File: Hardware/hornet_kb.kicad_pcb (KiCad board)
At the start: 2 copper layers, 195.1 x 100.9 mm, 133 parts, among them J1 Conn_ST_STDC14, J10 USB_C_Receptacle_USB2.0, J2 Conn_01x03, SW1 ESC, SW10 TAB, SW11 Q, SW12 W, SW13 E, SW14 R, SW15 T, SW17 M1, SW18 CAPS, SW19 A, SW2 `, SW20 S, SW21 D, SW22 F, SW23 G, SW25 M2, SW26 M3, SW28 SHIFT, SW29 CTRL, SW3 1, SW31 Z, SW32 WIN, SW34 X, SW35 FN, SW37 C, SW38 ALT, SW4 2, SW40 V, SW41 SPACE, SW43 B, SW44 DEL, SW5 3, SW6 4, SW7 5, SW8 6, SW9 M0, U1 nRF52840, U2 BQ24040, U3 BQ51050BRHL, U4 AP22814BW5, Y1 32.768kHz, Y2 32MHz

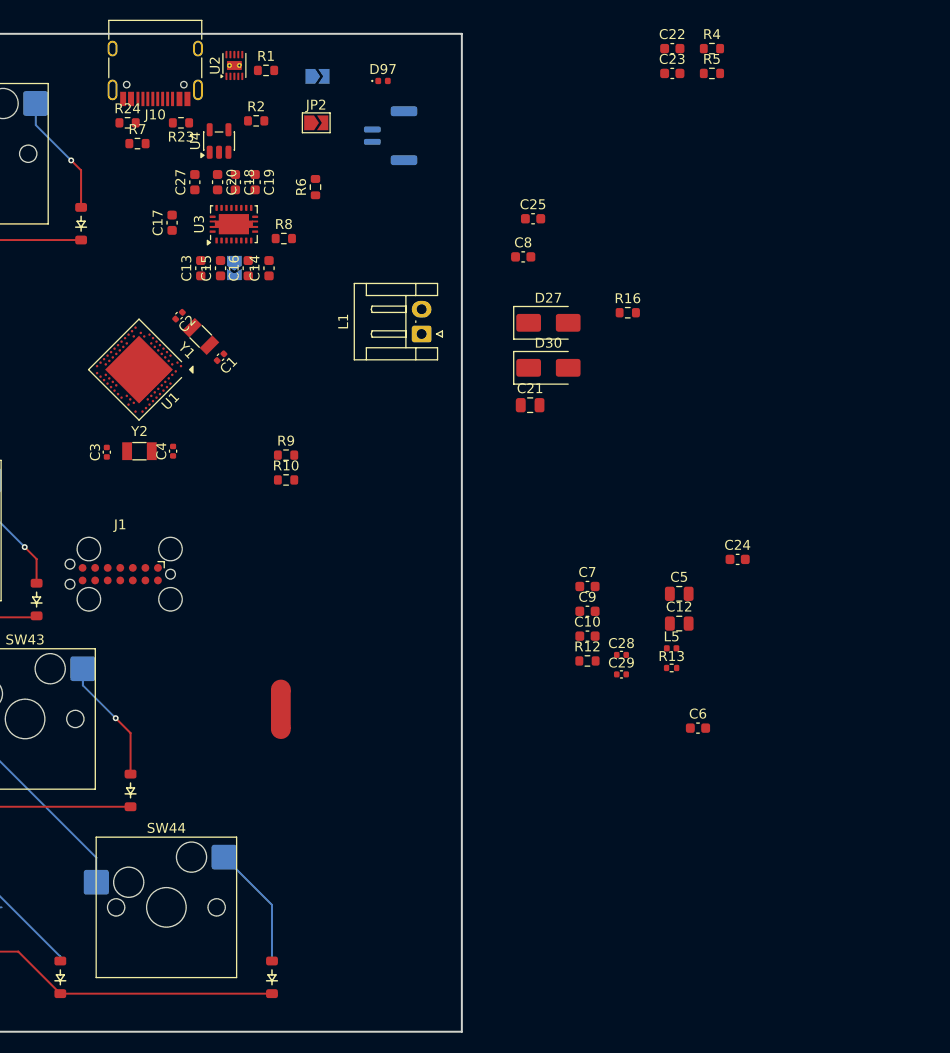
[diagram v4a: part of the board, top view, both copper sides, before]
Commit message: added extra decoupling caps to the mcu VDD pins
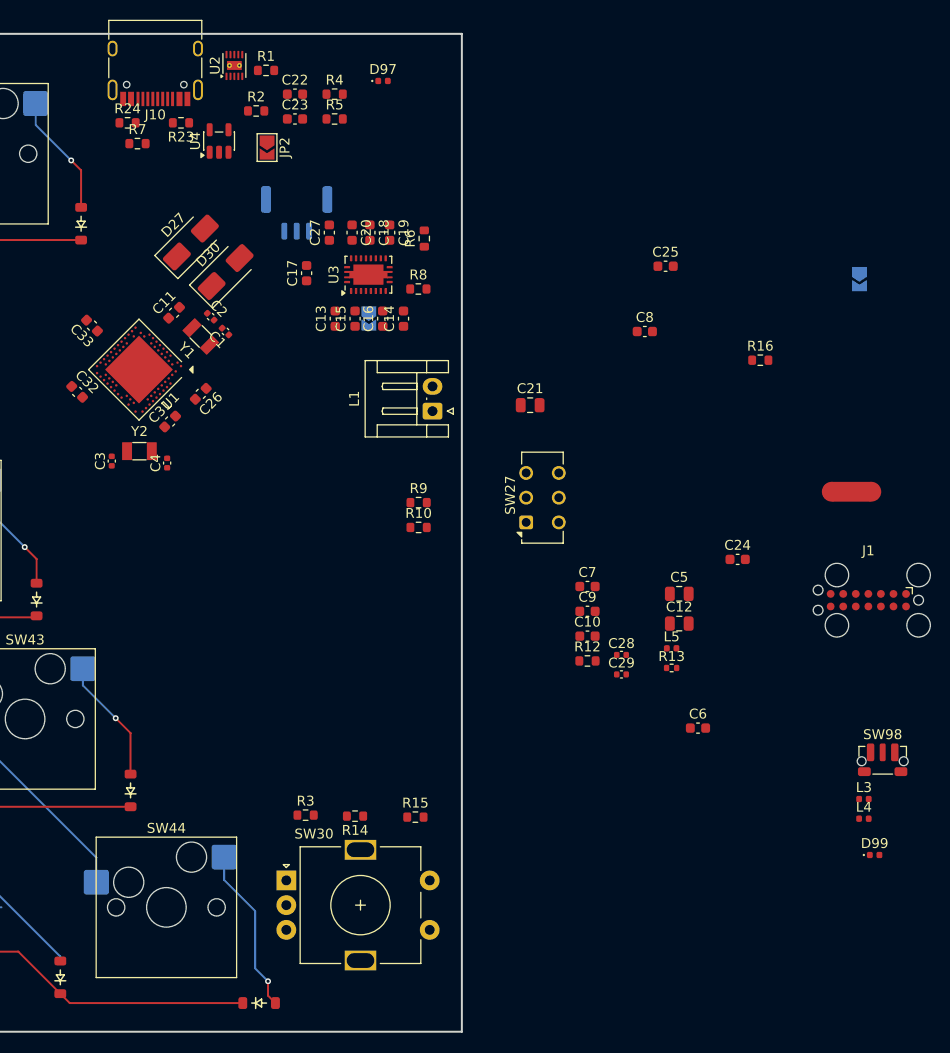
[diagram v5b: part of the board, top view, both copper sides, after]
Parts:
- added C11: 100pF, Capacitor_SMD:C_0603_1608Metric, F.Cu at (205.2, 73.2)
- added C26: 100pF, Capacitor_SMD:C_0603_1608Metric, F.Cu at (207.9, 81.4)
- added C31: 100pF, Capacitor_SMD:C_0603_1608Metric, F.Cu at (204.8, 84.2)
- added C32: 100pF, Capacitor_SMD:C_0603_1608Metric, F.Cu at (195.4, 81.2)
- added C33: 100pF, Capacitor_SMD:C_0603_1608Metric, F.Cu at (196.9, 74.5)
- added D99: QI_CHG, LED_SMD:LED_0402_1005Metric, F.Cu at (276.1, 128.1)
- added L3: 10uH, Inductor_SMD:L_0402_1005Metric, F.Cu at (275.0, 122.4)
- added L4: 25uH, Inductor_SMD:L_0402_1005Metric, F.Cu at (275.0, 124.4)
- added R14: 10k, Resistor_SMD:R_0603_1608Metric, F.Cu at (223.5, 124.1)
- added R15: 10k, Resistor_SMD:R_0603_1608Metric, F.Cu at (229.6, 124.2)
- added R3: 10k, Resistor_SMD:R_0603_1608Metric, F.Cu at (218.5, 124.0)
- added SW27: SW_DPDT_x2, Button_Switch_THT:SW_CK_JS202011CQN_DPDT_Straight, F.Cu at (240.8, 94.4)
- added SW30: Rot_Enc, Rotary_Encoder:RotaryEncoder_Alps_EC11E-Switch_Vertical_H20mm, F.Cu at (216.6, 130.6)
- added SW98: SW_Push, Button_Switch_SMD:SW_Push_1P1T-MP_NO_Horizontal_Alps_SKRTLAE010, F.Cu at (276.9, 118.6)
- C22: value 10uF -> 1uF
- J2: footprint Connector_JST:JST_GH_SM02B-GHS-TB_1x02-1MP_P1.25mm_Horizontal -> Connector_JST:JST_GH_SM03B-GHS-TB_1x03-1MP_P1.25mm_Horizontal
- moved J1 75.7 mm to (275.4, 102.3)
- moved NT1 61.8 mm to (273.7, 91.3), turned to 180 degrees
- moved JP1 58.5 mm to (274.5, 69.8), turned to -90 degrees
- moved C22 38.4 mm to (217.5, 51.1)
- moved C23 38.4 mm to (217.5, 53.6)
- moved R4 38.4 mm to (221.5, 51.1)
- moved R5 38.4 mm to (221.5, 53.6)
- moved D27 37.1 mm to (206.9, 66.1), turned to 45 degrees
- moved D30 34.0 mm to (210.5, 69.1), turned to 45 degrees
- moved C13 14.5 mm to (221.5, 73.8)
- moved C15 14.5 mm to (223.5, 73.8)
- moved C17 14.5 mm to (218.6, 69.2)
- moved U3 14.5 mm to (224.9, 69.4)
- moved C18 14.5 mm to (225.0, 65.1)
- moved C19 14.5 mm to (227.0, 65.1)
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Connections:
- C3 pad 1: GND1 -> GND
- C4 pad 1: GND1 -> GND
- U1 pad AC17: /R_COL_6 -> unconnected-(U1-P0.21-PadAC17)
- U1 pad AD10: unconnected-(U1-P0.15-PadAD10) -> /R_COL_7
- U1 pad AD12: unconnected-(U1-P0.17-PadAD12) -> /R_COL_6
- U1 pad AD16: /R_COL_7 -> /R_ROW_2
- U1 pad AD8: unconnected-(U1-P0.13-PadAD8) -> /R_ROW_0
- U1 pad V23: /R_ROW_2 -> unconnected-(U1-P1.03-PadV23)
- U1 pad Y23: /R_ROW_0 -> unconnected-(U1-P1.01-PadY23)
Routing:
- net Net-(D44-A): track 12.5 -> 16.9 mm, vias 0 -> 1
- net /R_ROW_4: track 156.1 -> 153.6 mm

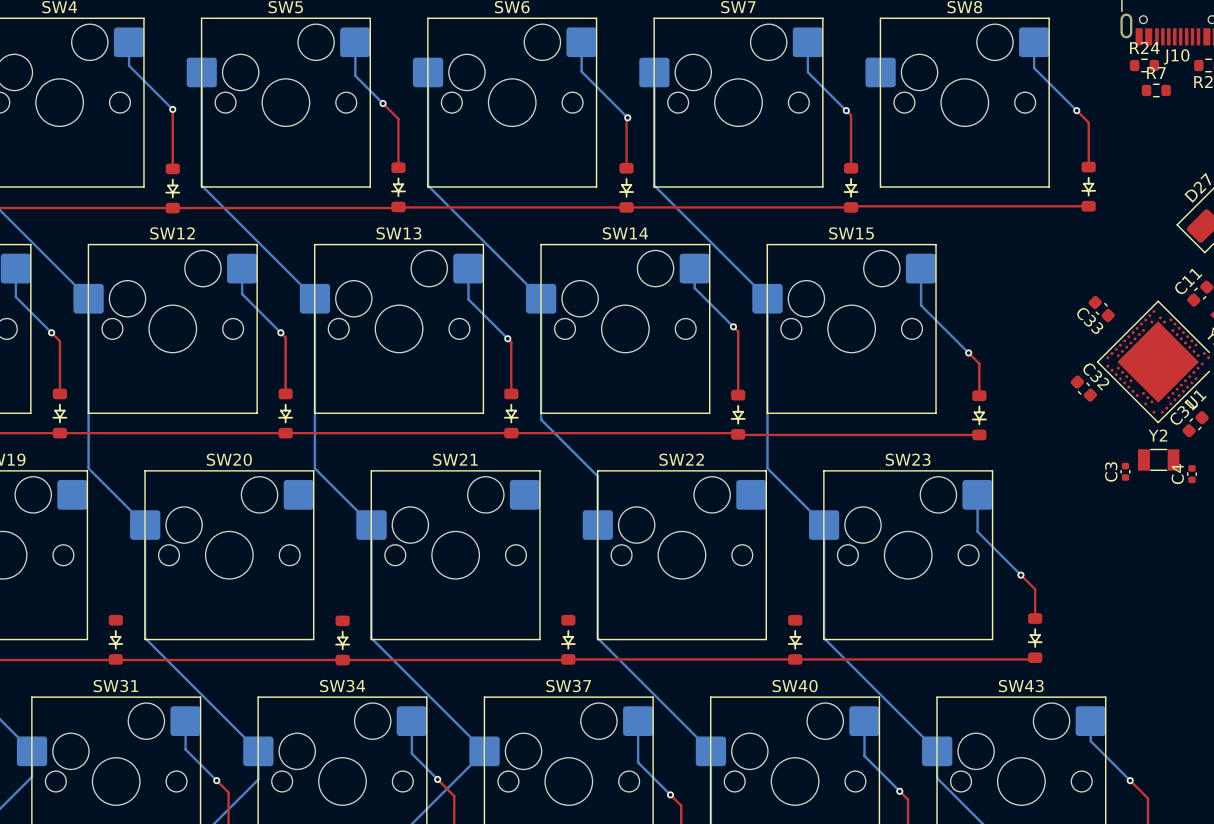
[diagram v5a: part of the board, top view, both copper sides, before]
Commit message: changed pin allocations for keys based on physical location
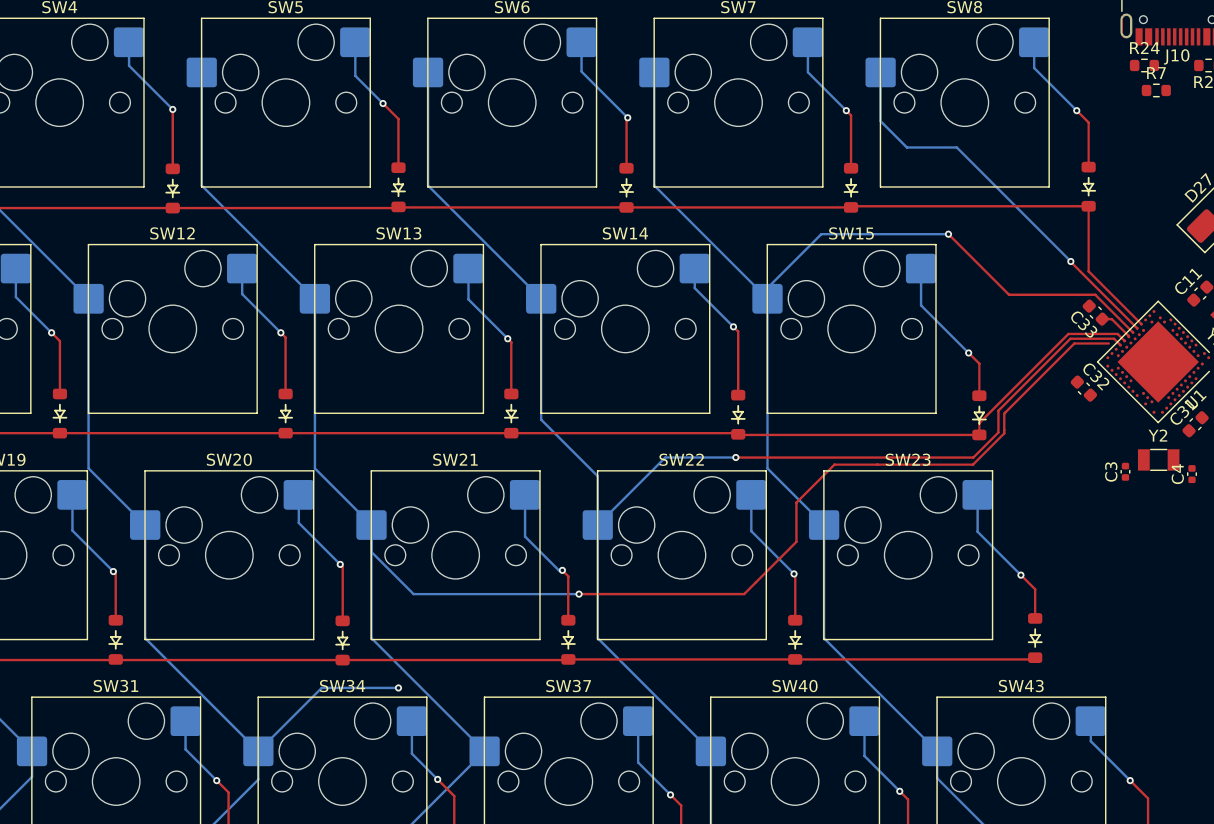
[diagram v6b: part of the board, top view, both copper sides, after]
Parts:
- moved C33 0.58 mm to (196.4, 74.8)
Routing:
- net /R_COL_4: track 91.0 -> 168.5 mm, vias 0 -> 1
- net /R_COL_5: track 87.0 -> 138.8 mm, vias 0 -> 1
- net /R_COL_6: track 92.0 -> 129.0 mm, vias 0 -> 1
- net /R_COL_7: track 0.00 -> 32.9 mm, vias 0 -> 1
- net /R_ROW_2: track 124.1 -> 140.7 mm
- net /R_COL_3: track 93.0 -> 107.0 mm, vias 0 -> 1
- net Net-(D21-A): track 0.00 -> 12.2 mm, vias 0 -> 1
- net Net-(D20-A): track 0.00 -> 12.1 mm, vias 0 -> 1
- net Net-(D22-A): track 0.00 -> 12.1 mm, vias 0 -> 1
- net Net-(D19-A): track 0.00 -> 12.1 mm, vias 0 -> 1
- net /R_ROW_0: track 134.4 -> 146.2 mm
- net VDD: track 0.00 -> 2.88 mm

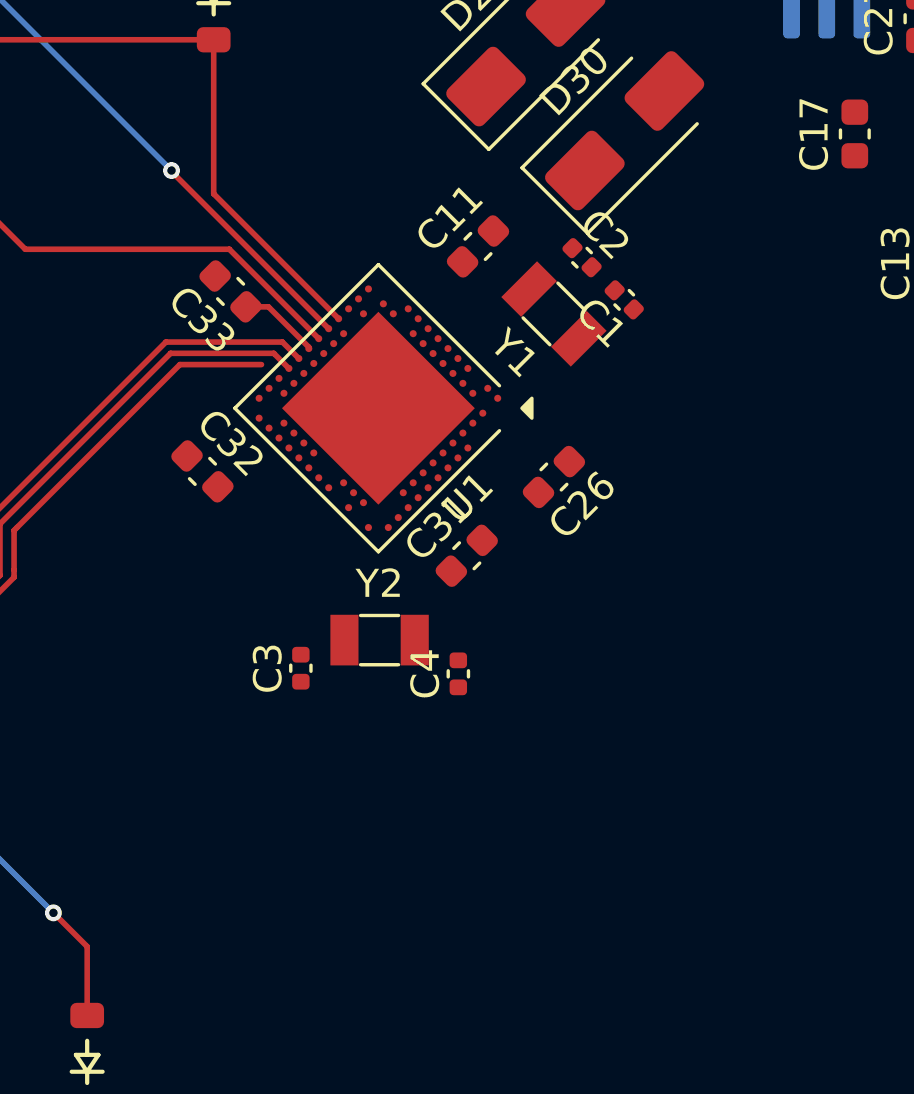
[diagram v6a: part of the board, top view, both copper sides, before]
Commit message: move MCU to prioritize BLE routing
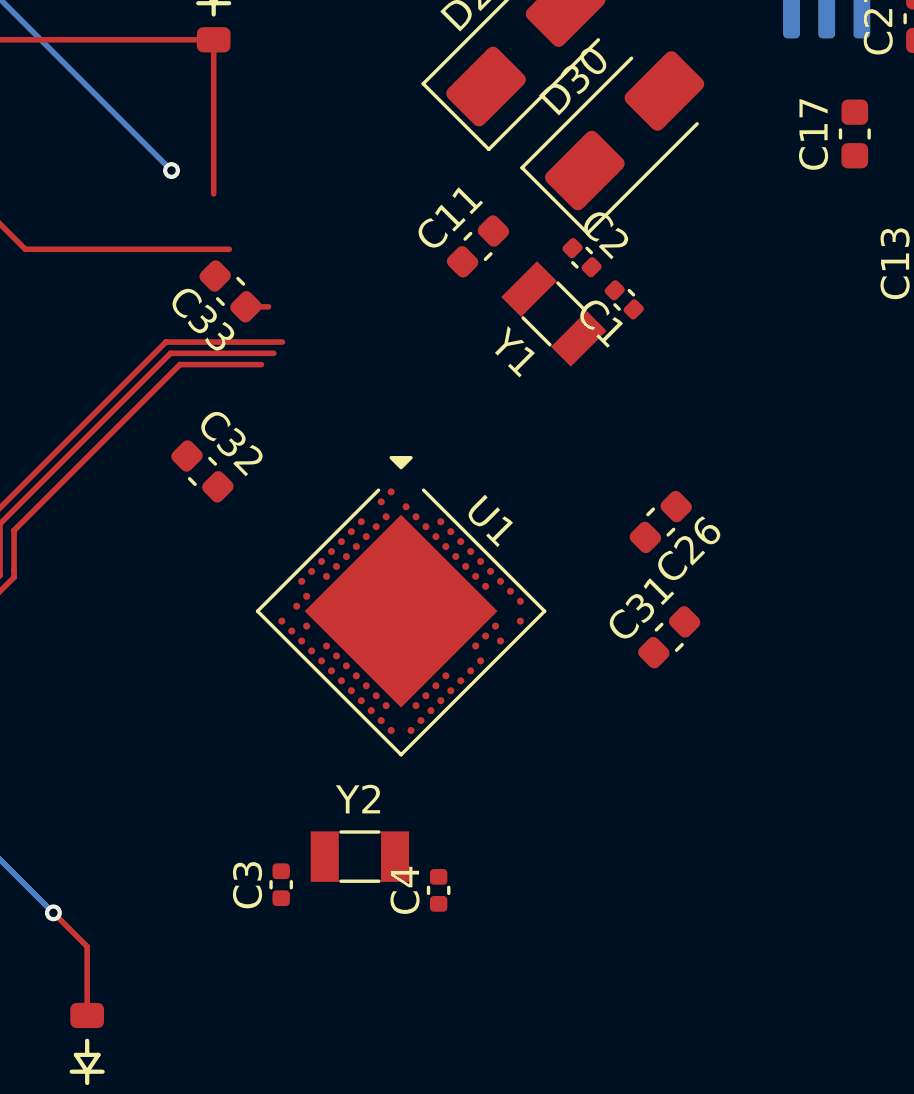
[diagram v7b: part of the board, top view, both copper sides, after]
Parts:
- moved C31 7.76 mm to (212.0, 87.1)
- moved Y2 7.73 mm to (201.0, 94.9)
- moved C3 7.73 mm to (198.2, 95.9)
- moved C4 7.73 mm to (203.8, 96.1)
- moved U1 7.26 mm to (202.5, 86.2), turned to -45 degrees
- moved C26 4.12 mm to (211.7, 83.0)
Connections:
- U1 pad AC19: /R_COL_4 -> unconnected-(U1-P0.23-PadAC19)
- U1 pad AD20: /R_COL_3 -> /R_COL_4
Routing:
- net /R_COL_7: track 32.9 -> 25.0 mm
- net /R_ROW_0: track 146.2 -> 139.9 mm
- net /R_COL_6: track 129.0 -> 124.5 mm
- net VDD: track 2.88 -> 0.80 mm
- net /R_ROW_2: track 140.7 -> 139.9 mm
- net /R_COL_5: track 138.8 -> 138.1 mm

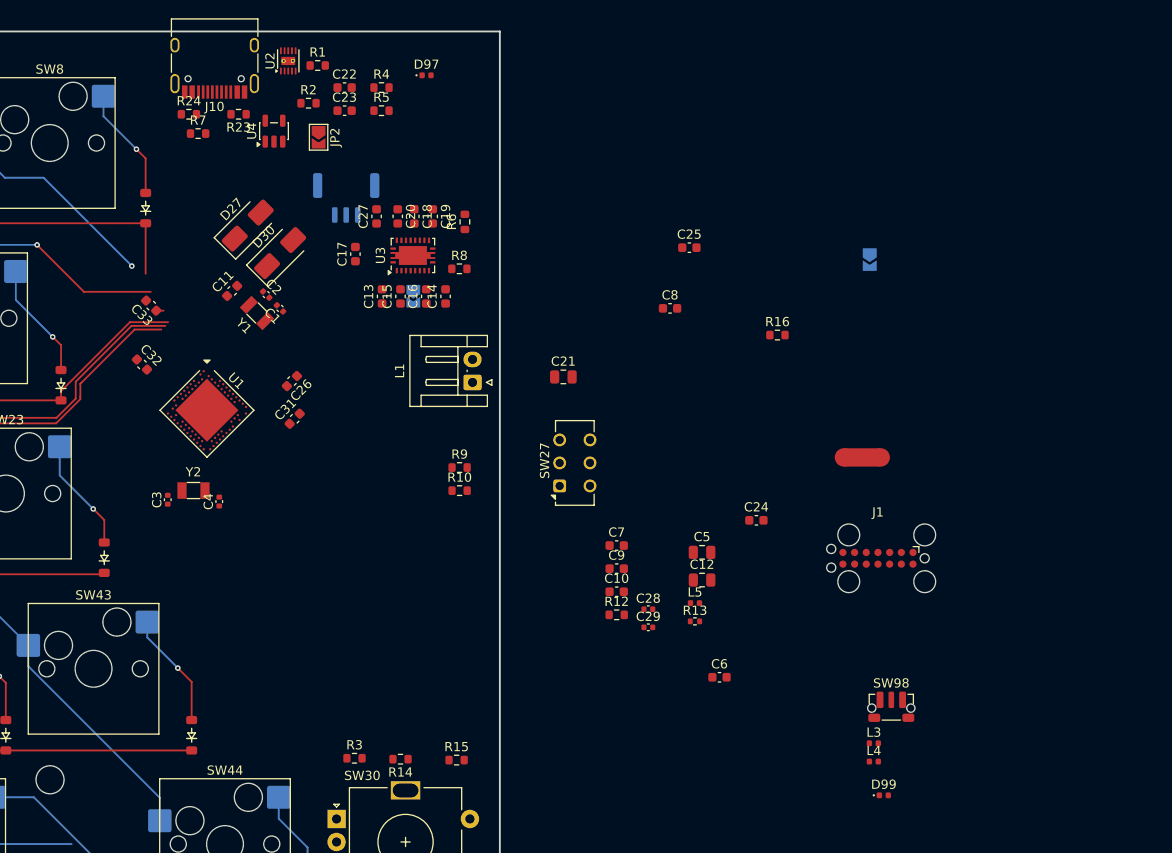
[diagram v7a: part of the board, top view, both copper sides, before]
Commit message: modified layout placement
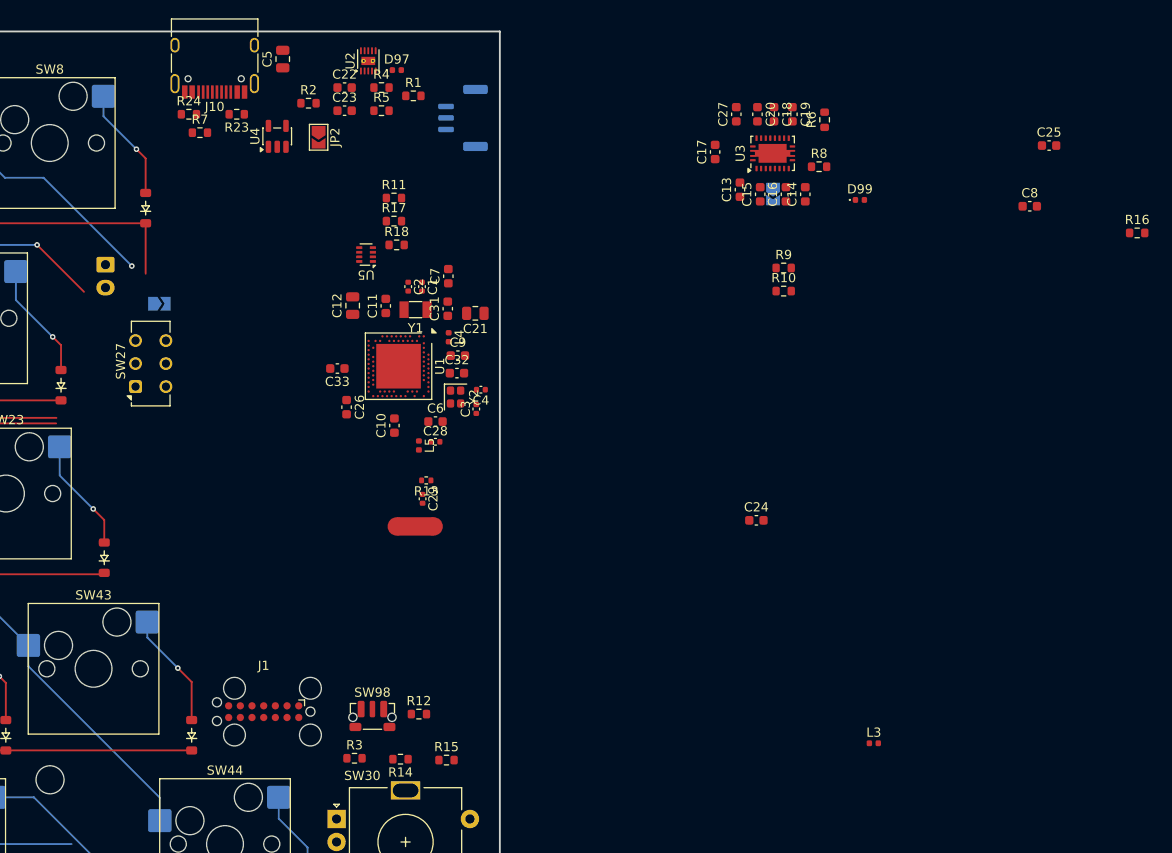
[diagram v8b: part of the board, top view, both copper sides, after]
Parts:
- removed D27, D30: SS14, Diode_SMD:D_SMA
- added R11: 1k, Resistor_SMD:R_0603_1608Metric, F.Cu at (222.8, 63.1)
- added R17: 20k, Resistor_SMD:R_0603_1608Metric, F.Cu at (222.8, 65.6)
- added R18: 1k, Resistor_SMD:R_0603_1608Metric, F.Cu at (223.1, 68.2)
- added U5: TPS2116DRL, Package_TO_SOT_SMD:SOT-583-8, F.Cu at (219.8, 69.3)
- L1: moved to B.Cu
- Y2: footprint Crystal:Crystal_SMD_3215-2Pin_3.2x1.5mm -> Crystal:Crystal_SMD_2016-4Pin_2.0x1.6mm
- moved JP1 77.3 mm to (197.3, 74.6), turned to 0 degrees
- moved C5 70.4 mm to (210.7, 48.0), turned to 90 degrees
- moved J1 68.8 mm to (208.7, 119.0)
- moved L4 65.3 mm to (228.8, 78.3), turned to -90 degrees
- moved D99 64.8 mm to (273.5, 63.3)
- moved SW98 56.4 mm to (220.5, 119.6)
- moved NT1 49.2 mm to (225.1, 98.8)
- moved C12 48.3 mm to (218.3, 74.8), turned to 90 degrees
- moved SW27 47.3 mm to (194.7, 83.6)
- moved L1 41.9 mm to (191.5, 70.4), turned to -90 degrees
- moved C6 41.5 mm to (227.3, 87.4)
- moved R10 41.4 mm to (265.2, 73.2)
- moved R9 41.4 mm to (265.2, 70.7)
- moved R16 40.6 mm to (303.6, 66.9)
- moved C14 40.6 mm to (267.5, 62.7)
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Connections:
- net Net-(U1-ANT) renamed /ANT
- C21 pad 1: VDD -> GND
- C21 pad 2: GND -> VDD
- U1 pad A14: /COMPRT_TX -> unconnected-(U1-P1.15-PadA14)
- U1 pad B15: /COMPRT_RX -> unconnected-(U1-P1.14-PadB15)
- U1 pad Y2: Net-(D27-K) -> VDDH
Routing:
- net /R_COL_5: track 138.1 -> 121.0 mm
- net /R_COL_4: track 168.5 -> 151.8 mm
- net /R_ROW_2: track 139.9 -> 124.1 mm
- net /R_COL_6: track 124.5 -> 117.2 mm
- net VDD: track 0.80 -> 0.00 mm
